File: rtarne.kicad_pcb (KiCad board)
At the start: 2 copper layers, 0 parts

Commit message: Add PCB elements. Update pin and add connect pin from footprint
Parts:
- added J1: 4PIN, kbd:MJ-4PP-9_1side, F.Cu at (119.4, 78.1)
- added J2: OLED, kbd:OLED, F.Cu at (37.2, 116.3)
- added J3: LED, kbd:StripLED_rev, F.Cu at (136.1, 61.5)
- added JP1: , kbd:Jumper, F.Cu at (58.7, 115.9)
- added JP2: , kbd:Jumper, F.Cu at (55.3, 115.9)
- added JP3: , kbd:Jumper, F.Cu at (51.9, 115.9)
- added JP4: , kbd:Jumper, F.Cu at (48.4, 115.9)
- added RSW1: SW_RST, kbd:ResetSW_1side, F.Cu at (72.4, 113.8)
- added SW_4: Switch, RTA-80:SW_RTA80, F.Cu at (107.9, 85.9)
- added SW_A1: Switch, RTA-80:SW_RTA80, F.Cu at (110.7, 51.7)
- added SW_C1: Switch, RTA-80:SW_RTA80, F.Cu at (159.0, 51.7)
- added SW_CH1: Switch, RTA-80:SW_RTA80, F.Cu at (110.7, 68.8)
- added SW_Ctrl1: Switch, RTA-80:SW_RTA80, F.Cu at (142.9, 51.7)
- added SW_E1: Switch, RTA-80:SW_RTA80, F.Cu at (107.9, 103.0)
- added SW_F1: Switch, RTA-80:SW_RTA80, F.Cu at (126.8, 68.8)
- added SW_I1: Switch, RTA-80:SW_RTA80, F.Cu at (62.4, 68.8)
- added SW_J1: Switch, RTA-80:SW_RTA80, F.Cu at (43.5, 88.8)
- added SW_K1: Switch, RTA-80:SW_RTA80, F.Cu at (59.6, 105.9)
- added SW_M1: Switch, RTA-80:SW_RTA80, F.Cu at (59.6, 88.8)
- added SW_MOD1: Switch, RTA-80:SW_RTA80, F.Cu at (43.5, 105.9)
- added SW_N1: Switch, RTA-80:SW_RTA80, F.Cu at (75.7, 85.9)
- added SW_P1: Switch, RTA-80:SW_RTA80, F.Cu at (94.6, 51.7)
- added SW_Q1: Switch, RTA-80:SW_RTA80, F.Cu at (126.8, 51.7)
- added SW_S1: Switch, RTA-80:SW_RTA80, F.Cu at (78.5, 68.8)
- added SW_Shift1: Switch, RTA-80:SW_RTA80, F.Cu at (91.8, 103.0)
- added SW_Space1: Switch, RTA-80:SW_RTA80, F.Cu at (78.5, 51.7)
- added SW_TAB1: Switch, RTA-80:SW_RTA80, F.Cu at (62.4, 51.7)
- added SW_U1: Switch, RTA-80:SW_RTA80, F.Cu at (75.7, 103.0)
- added SW_W1: Switch, RTA-80:SW_RTA80, F.Cu at (94.6, 68.8)
- added SW_Y1: Switch, RTA-80:SW_RTA80, F.Cu at (91.8, 85.9)
- added U1: ProMicro, kbd:ProMicro_v3, F.Cu at (44.9, 64.9)
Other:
- net class Default removed

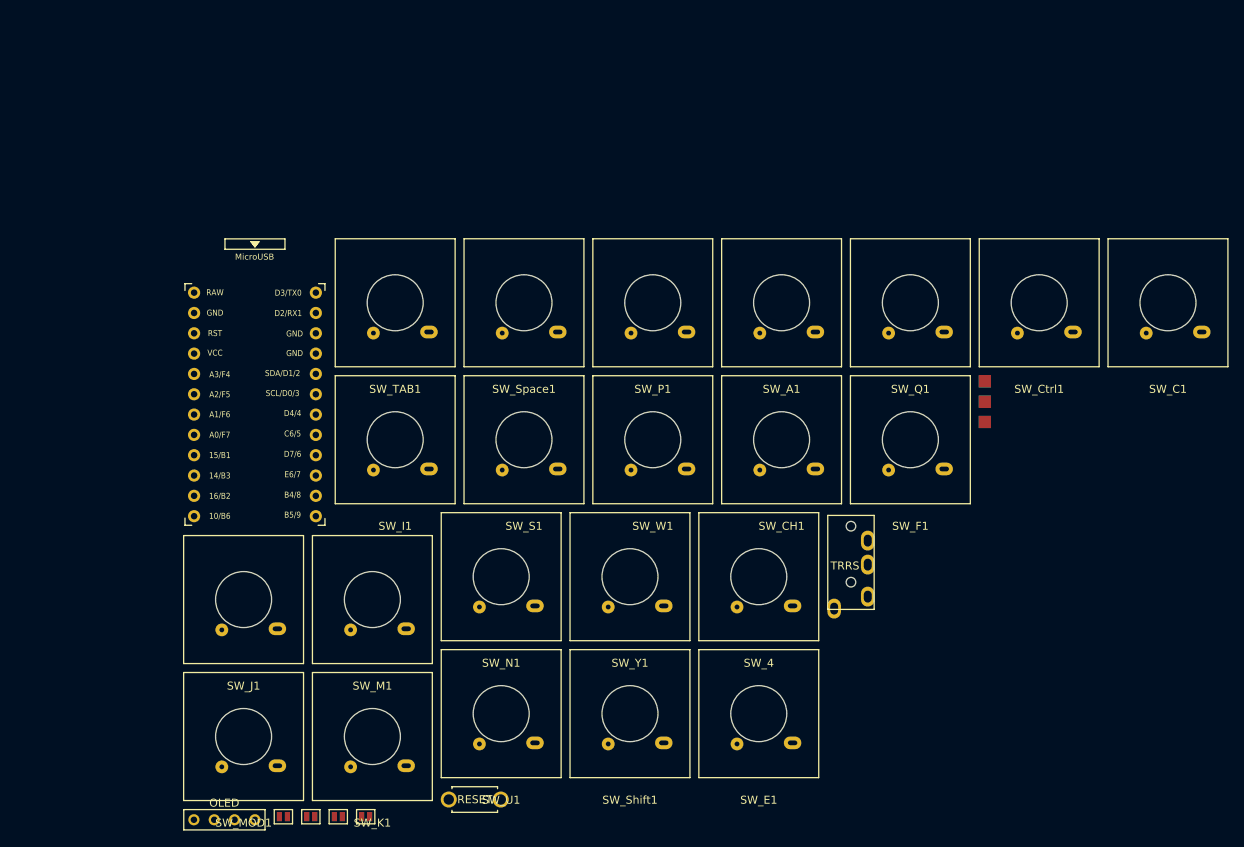
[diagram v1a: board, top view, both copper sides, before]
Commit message: Add edge cut and set switch case plase
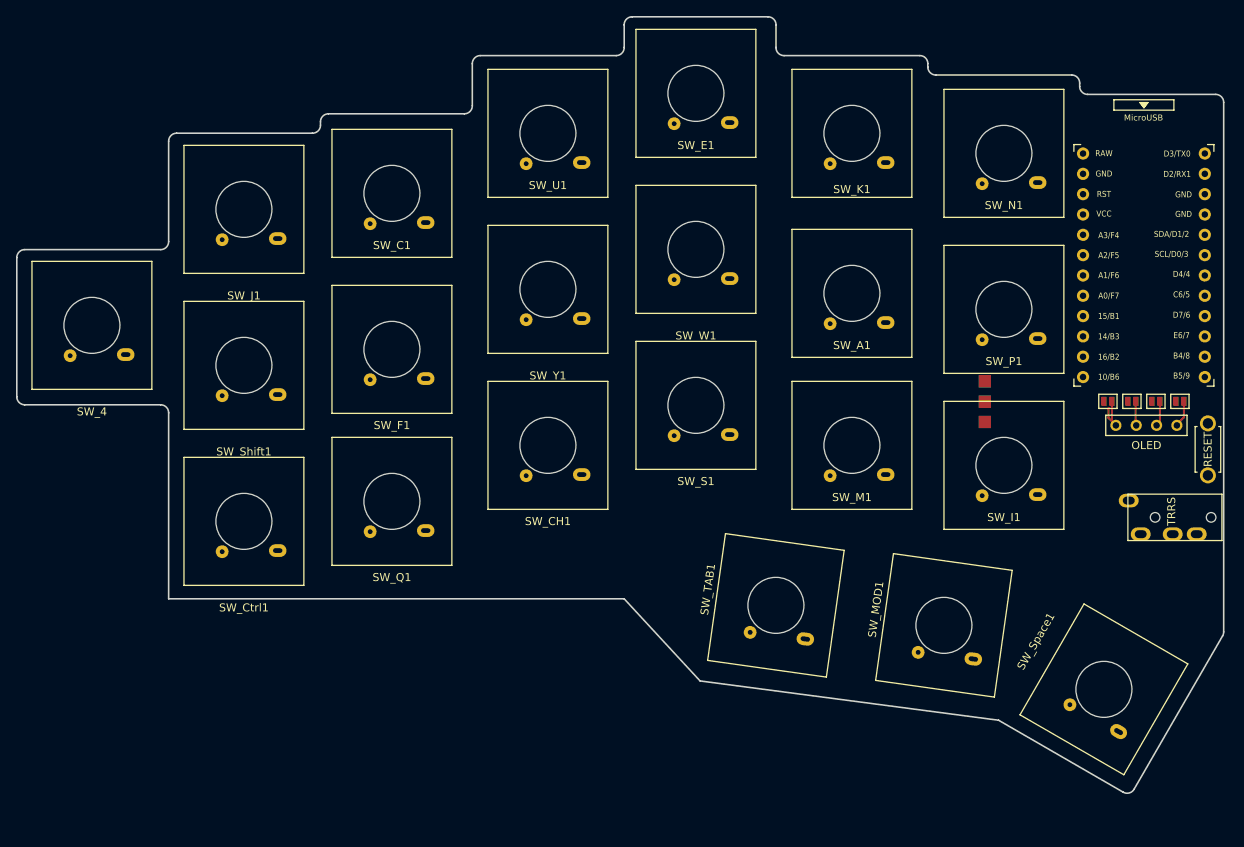
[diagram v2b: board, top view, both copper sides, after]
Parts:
- moved J2 125.4 mm to (152.5, 67.0)
- moved JP4 115.4 mm to (151.5, 64.0)
- moved JP3 115.0 mm to (154.5, 64.0)
- moved JP2 114.6 mm to (157.5, 64.0)
- moved JP1 114.3 mm to (160.5, 64.0)
- moved U1 112.5 mm to (156.0, 47.5)
- moved SW_Ctrl1 103.1 mm to (43.5, 79.0)
- moved RSW1 101.6 mm to (164.0, 70.0), turned to -90 degrees
- moved SW_C1 98.0 mm to (62.0, 38.0)
- moved SW_K1 96.3 mm to (119.5, 30.5)
- moved SW_4 89.1 mm to (24.5, 54.5)
- moved SW_MOD1 88.6 mm to (131.0, 92.0), turned to -8 degrees
- moved SW_Space1 87.1 mm to (151.0, 100.0), turned to -30 degrees
- moved SW_N1 82.2 mm to (138.5, 33.0)
- moved SW_E1 77.9 mm to (100.0, 25.5)
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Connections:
- J1 pad A: unconnected-(J1-PadA) -> (no net)
- SW_K1 pad 2: unconnected-(SW_K1-Pad2) -> (no net)
- SW_S1 pad 2: unconnected-(SW_S1-Pad2) -> (no net)
- SW_TAB1 pad 2: unconnected-(SW_TAB1-Pad2) -> (no net)
- SW_U1 pad 2: unconnected-(SW_U1-Pad2) -> (no net)
- SW_W1 pad 2: unconnected-(SW_W1-Pad2) -> (no net)
- U1 pad 12: unconnected-(U1-Pad12) -> (no net)
- U1 pad 19: unconnected-(U1-Pad19) -> (no net)
- U1 pad 20: unconnected-(U1-Pad20) -> (no net)
- U1 pad 24: unconnected-(U1-Pad24) -> (no net)
- U1 pad 7: unconnected-(U1-Pad7) -> (no net)
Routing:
- net Net-(J2-Pad1): track 0.00 -> 5.79 mm
- net Net-(J2-Pad2): track 0.00 -> 3.57 mm
- net Net-(J2-Pad4): track 0.00 -> 3.41 mm
- net Net-(J2-Pad3): track 0.00 -> 3.21 mm
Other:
- board outline added: 150.9 x 97.1 mm
